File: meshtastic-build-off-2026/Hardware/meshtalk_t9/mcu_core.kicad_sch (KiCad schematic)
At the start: 6 parts, among them SW1 SW_Push, U1 ESP32-S3-WROOM-1

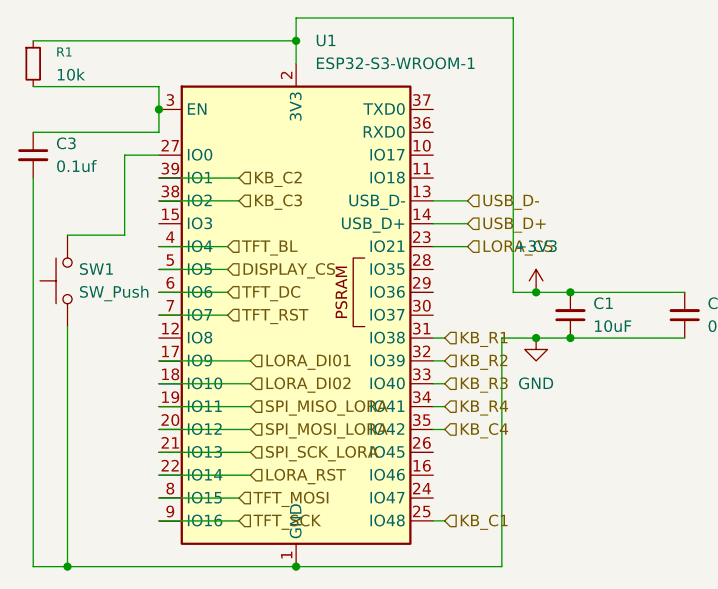
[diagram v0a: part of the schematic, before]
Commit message: rename + battery % + boot btn changed to reset + fix battery chrging
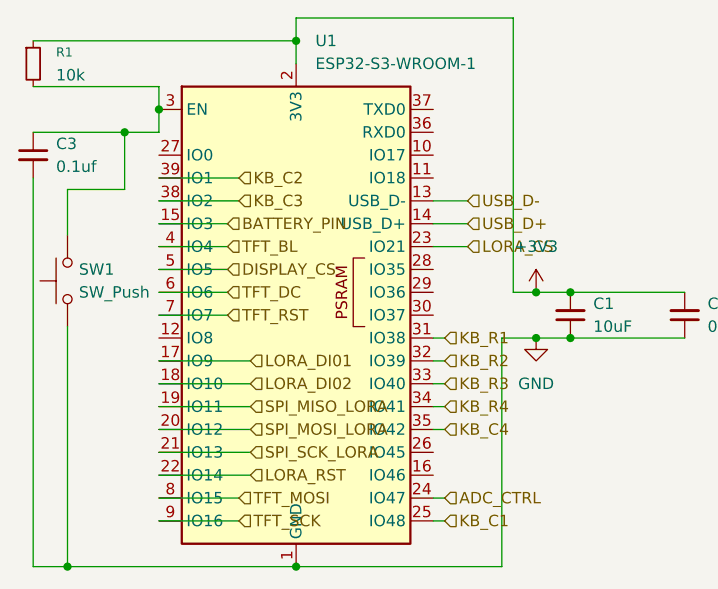
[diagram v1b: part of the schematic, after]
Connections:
- net at SW1.2: now also C3.1, R1.2, U1.3 (EN); no longer U1.27 (IO0)
- net BATTERY_PIN: now reaches U1.15 (IO3)
- net ADC_CTRL: now reaches U1.24 (IO47)
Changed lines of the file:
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@@
+	)
+	(junction
+		(at 49.53 54.61)
+		(diameter 0)
+		(color 0 0 0 0)
 	)
 	(junction
@@
 	(wire
 		(pts
+			(xy 49.53 54.61) (xy 53.34 54.61)
+		)
+		(stroke
+			(width 0)
+			(type default)
+		)
+	)
+	(wire
+		(pts
 			(xy 53.34 72.39) (xy 60.96 72.39)
 		)
@@
 	(wire
 		(pts
-			(xy 43.18 66.04) (xy 49.53 66.04)
-		)
-		(stroke
-			(width 0)
-			(type default)
-		)
-	)
-	(wire
-		(pts
 			(xy 91.44 77.47) (xy 95.25 77.47)
 		)
@@
 	(wire
 		(pts
-			(xy 49.53 66.04) (xy 49.53 57.15)
+			(xy 43.18 66.04) (xy 43.18 60.96)
 		)
 		(stroke
@@
 	(wire
 		(pts
-			(xy 49.53 57.15) (xy 53.34 57.15)
-		)
-		(stroke
-			(width 0)
-			(type default)
-		)
-	)
-	(wire
-		(pts
 			(xy 83.82 64.77) (xy 87.63 64.77)
 		)
@@
 	(wire
 		(pts
-			(xy 39.37 54.61) (xy 53.34 54.61)
+			(xy 39.37 54.61) (xy 49.53 54.61)
 		)
 		(stroke
@@
 	(wire
 		(pts
+			(xy 43.18 60.96) (xy 49.53 60.96)
+		)
+		(stroke
+			(width 0)
+			(type default)
+		)
+	)
+	(wire
+		(pts
 			(xy 53.34 67.31) (xy 60.96 67.31)
 		)
@@
 	(wire
 		(pts
+			(xy 49.53 60.96) (xy 49.53 54.61)
+		)
+		(stroke
+			(width 0)
+			(type default)
+		)
+	)
+	(wire
+		(pts
 			(xy 68.58 41.91) (xy 92.71 41.91)
 		)
@@
 	(wire
 		(pts
+			(xy 83.82 95.25) (xy 85.09 95.25)
+		)
+		(stroke
+			(width 0)
+			(type default)
+		)
+	)
+	(wire
+		(pts
 			(xy 91.44 102.87) (xy 91.44 77.47)
 		)
@@
 	(wire
 		(pts
+			(xy 53.34 64.77) (xy 60.96 64.77)
+		)
+		(stroke
+			(width 0)
+			(type default)
+		)
+	)
+	(wire
+		(pts
 			(xy 95.25 77.47) (xy 99.06 77.47)
 		)
@@
 		)
 	)
+	(hierarchical_label "BATTERY_PIN"
+		(shape input)
+		(at 60.96 64.77 0)
+		(effects
+			(font
+				(size 1.27 1.27)
+			)
+			(justify left)
+		)
+	)
+	(hierarchical_label "ADC_CTRL"
+		(shape input)
+		(at 85.09 95.25 0)
+		(effects
+			(font
+				(size 1.27 1.27)
+			)
+			(justify left)
+		)
+	)

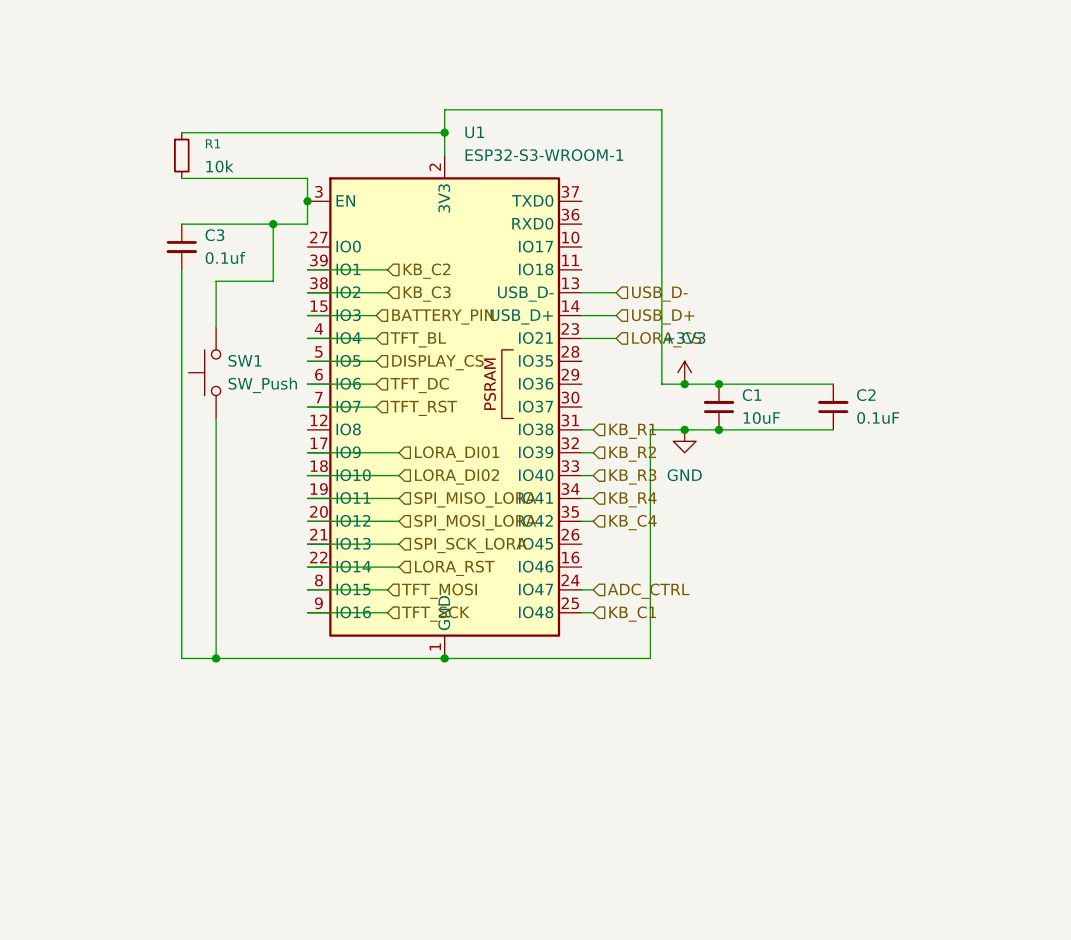
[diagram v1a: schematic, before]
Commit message: Replace AP2112K-3.3  with AP7361C-33E Connected LORA RF_SW1 to GPIO Added ESD Added mounting holes for display (Waveshare 2 inch) Added Boot and Reset buttons made power rails thicker added dedicated layer for 3v3 and GND
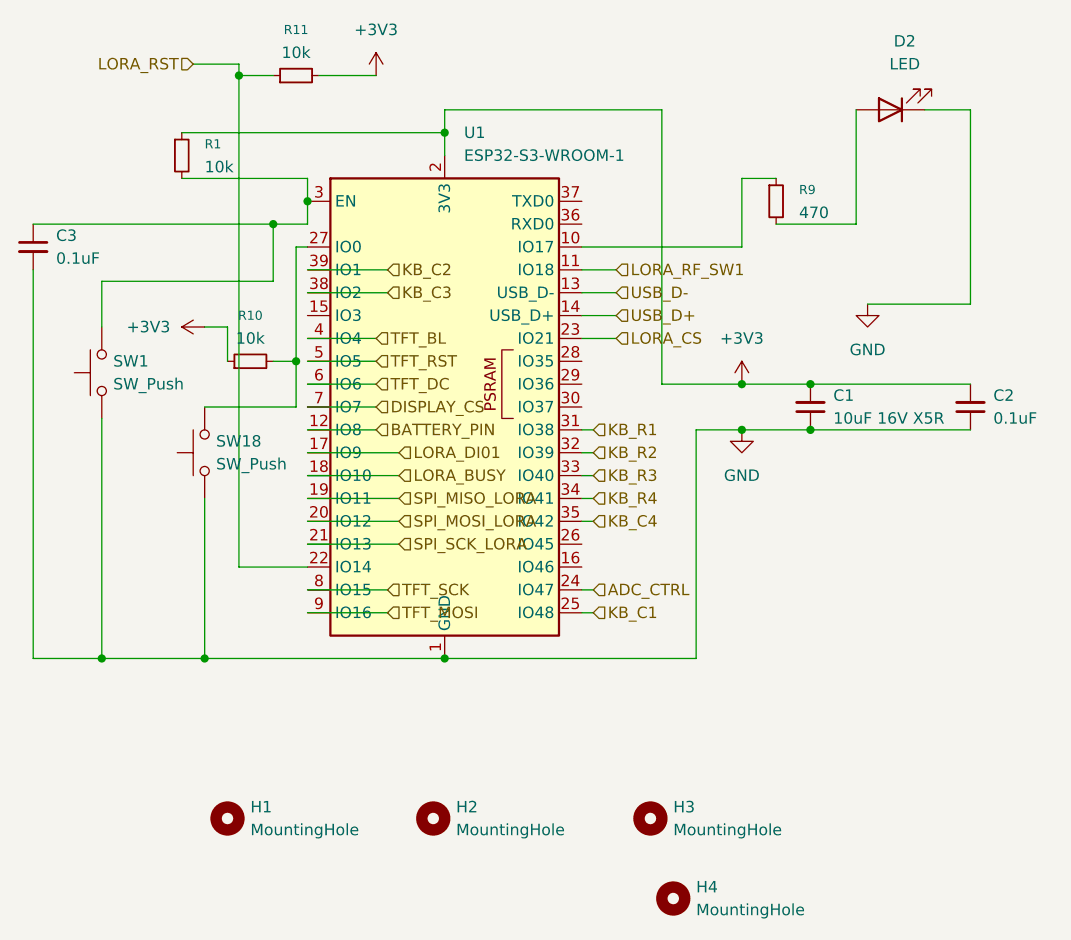
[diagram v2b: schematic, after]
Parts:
- added D2: LED, LED_SMD:LED_0805_2012Metric, symbol Device:LED
- added H1, H2, H3, H4: MountingHole, MountingHole:MountingHole_2.2mm_M2, symbol Mechanical:MountingHole
- added R10, R11: 10k, Resistor_SMD:R_0805_2012Metric, symbol Device:R_Small
- added R9: 470, Resistor_SMD:R_0805_2012Metric, symbol Device:R_Small
- added SW18: SW_Push, Button_Switch_SMD:SW_Push_1P1T_NO_CK_KMR2, symbol Switch:SW_Push
- C1: value 10uF -> 10uF 16V X5R; MPN (none) -> CL21A106KOQNNNE; Manufacturer (none) -> Samsung
- C2: MPN (none) -> CC0805KRX7R9BB104; Manufacturer (none) -> YAGEO
- C3: value 0.1uf -> 0.1uF; MPN (none) -> CC0805KRX7R9BB104; Manufacturer (none) -> YAGEO
- R1: MPN (none) -> RC0805FR-0710KL; Manufacturer (none) -> YAGEO
- SW1: footprint Button_Switch_SMD:SW_SPST_Omron_B3FS-100xP -> Button_Switch_SMD:SW_Push_1P1T_NO_CK_KMR2; MPN (none) -> KMR221G LFS; Manufacturer (none) -> HROparts
- U1: MPN (none) -> ESP32-S3-WROOM-1-N16R16VA; Manufacturer (none) -> Espressif
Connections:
- net +3V3: now also R10.1, R11.2
- net BATTERY_PIN: now also U1.12 (IO8); no longer U1.15 (IO3)
- net DISPLAY_CS: now also U1.7 (IO7); no longer U1.5 (IO5)
- net GND: now also D2.1 (K), SW18.1
- net LORA_RST: now also R11.1
- net TFT_MOSI: now also U1.9 (IO16); no longer U1.8 (IO15)
- net TFT_RST: now also U1.5 (IO5); no longer U1.7 (IO7)
- net TFT_SCK: now also U1.8 (IO15); no longer U1.9 (IO16)
- net at U1.10 (IO17): now also R9.1
- net LORA_RF_SW1: now reaches U1.11 (IO18)
- net at U1.27 (IO0): now also R10.2, SW18.2
- net LORA_DI02 renamed LORA_BUSY
- new net: D2.2 (A), R9.2
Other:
- moved on the sheet: C1, C2, C3, SW1

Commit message: PCB Updates - Align net names Clearence for esp32 antenna
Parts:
- U1: MPN ESP32-S3-WROOM-1-N16R16VA -> ESP32-S3-WROOM-1-N16R8
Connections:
- net DISPLAY_CS renamed TFT_CS
- net TFT_SCK renamed TFT_CLK
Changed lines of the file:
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@@
 		)
 	)
-	(hierarchical_label "TFT_SCK"
+	(hierarchical_label "TFT_CLK"
 		(shape input)
 		(at 62.23 95.25 0)
@@
 		)
 	)
-	(hierarchical_label "DISPLAY_CS"
+	(hierarchical_label "TFT_CS"
 		(shape input)
 		(at 60.96 74.93 0)
@@
 			)
 		)
-		(property "MPN" "ESP32-S3-WROOM-1-N16R16VA"
+		(property "MPN" "ESP32-S3-WROOM-1-N16R8"
 			(at 68.58 74.93 0)
 			(effects
